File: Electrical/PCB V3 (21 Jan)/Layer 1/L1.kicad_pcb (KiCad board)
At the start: 2 copper layers, 178 x 170 mm, 197 parts, among them J1 Conn_01x04, U2 CD74HC4067SM, U3 CD74HC4067SM, U5 113991054

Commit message: fixed l1 and l3, awaiting vetting
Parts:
- moved LED20 0.30 mm to (141.7, 149.5)
- moved LED12 0.30 mm to (72.0, 135.7)
- moved LED28 0.30 mm to (155.5, 79.9)
- moved LED4 0.30 mm to (85.9, 66.0)
- moved L10 0.30 mm to (67.7, 117.0)
- moved L18 0.30 mm to (122.9, 153.9)
- moved LED26 0.30 mm to (163.0, 98.0)
- moved L2 0.30 mm to (104.6, 61.7)
- moved LED10 0.30 mm to (64.5, 117.6)
- moved LED2 0.30 mm to (104.0, 58.5)
- moved L26 0.30 mm to (159.9, 98.6)
- moved LED18 0.30 mm to (123.6, 157.0)
- moved L31 0.30 mm to (131.8, 64.4)
- moved L15 0.30 mm to (95.8, 151.2)
- moved L23 0.30 mm to (157.2, 125.8)
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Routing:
- net /L1 RX: track 30.8 -> 43.0 mm
- net +3V3: track 163.9 -> 153.5 mm
- net Net-(L29-Pad2): track 4.43 -> 5.33 mm
- net GND: vias 10 -> 238

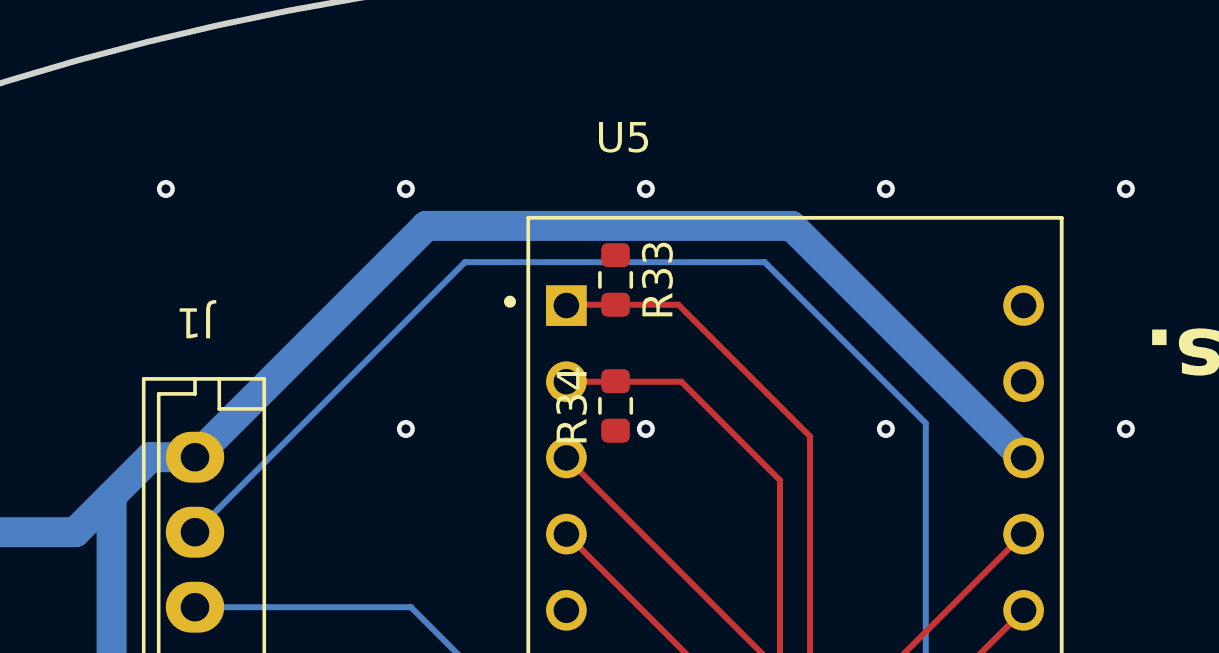
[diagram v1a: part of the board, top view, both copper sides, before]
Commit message: L1 & L3 APPROVED BY HAOYUN
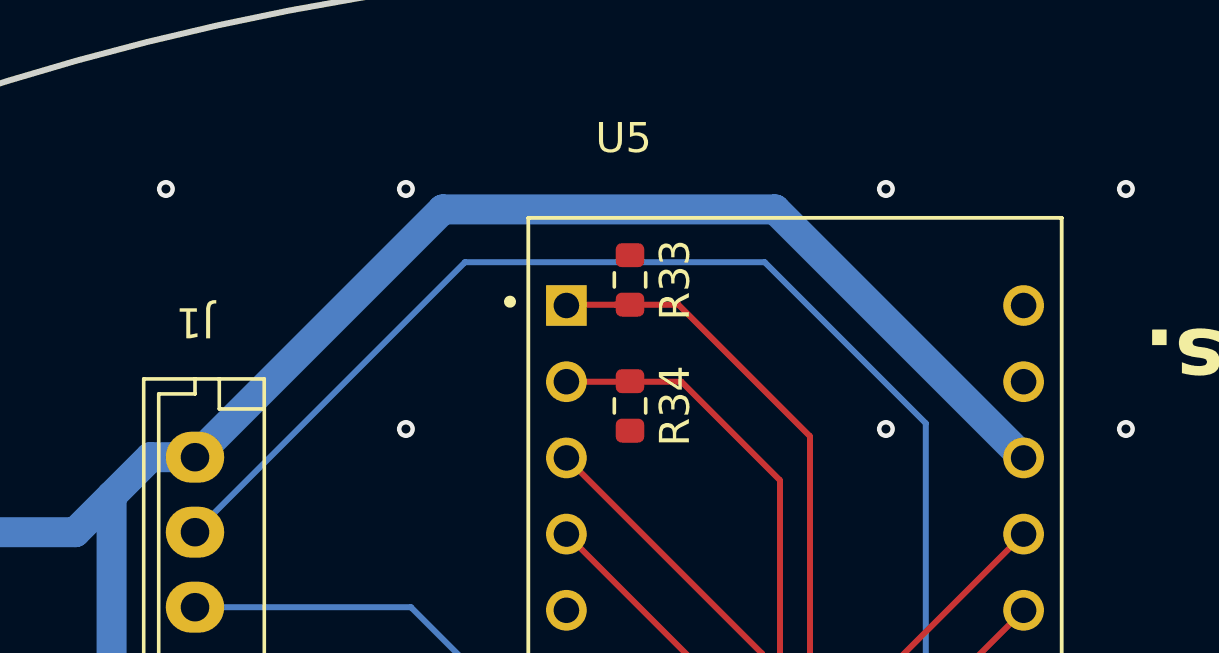
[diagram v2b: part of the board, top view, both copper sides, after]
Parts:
- moved R33 0.48 mm to (108.3, 29.4)
- moved R34 0.48 mm to (108.3, 33.6)
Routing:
- net GND: vias 238 -> 236

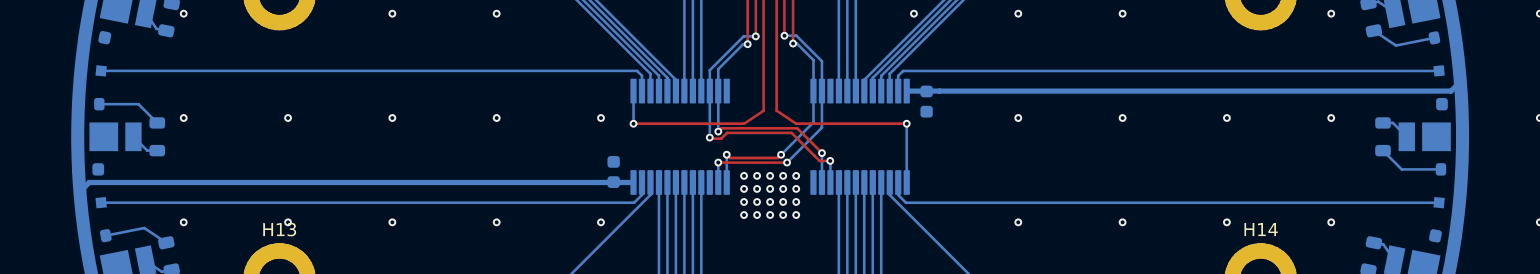
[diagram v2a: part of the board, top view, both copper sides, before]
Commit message: fixed l1 and l3
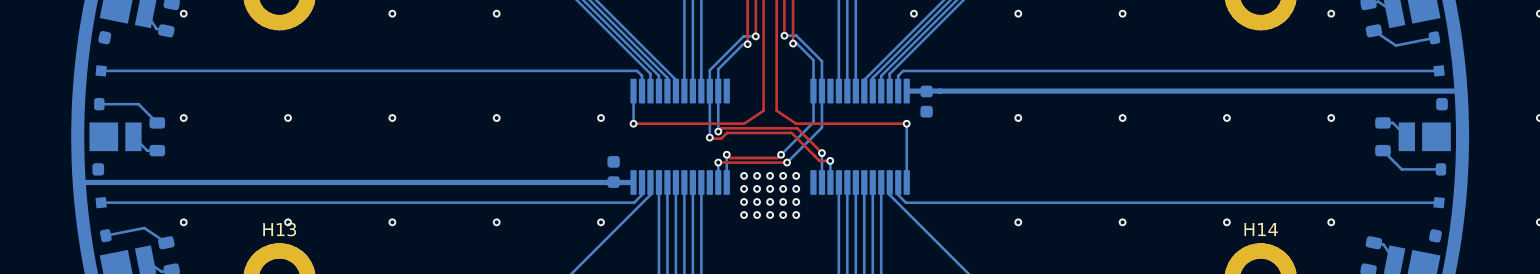
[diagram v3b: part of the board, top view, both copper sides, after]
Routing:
- net +3V3: track 154.0 -> 153.1 mm
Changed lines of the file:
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@@
-	)
-	(segment
-		(start 166.609377 103.65432)
-		(end 165.984377 104.27932)
-		(width 0.4)
-		(layer "B.Cu")
-		(net 2)
 	)
 	(segment
@@
 	)
 	(segment
-		(start 61.554377 111.28932)
+		(start 61.169377 111.28932)
 		(end 103.294374 111.28932)
 		(width 0.4)
@@
 	)
 	(segment
-		(start 60.909377 111.93432)
-		(end 61.554377 111.28932)
-		(width 0.4)
-		(layer "B.Cu")
-		(net 2)
-	)
-	(segment
 		(start 90.989377 59.546741)
 		(end 91.148756 59.70612)
@@
 	)
 	(segment
-		(start 165.984377 104.27932)
+		(start 166.469377 104.27932)
 		(end 126.769377 104.27932)
 		(width 0.4)
@@
 		(layers "F&B.Cu")
 		(hatch edge 0.5)
-		(connect_pads
-			(clearance 0.15)
+		(connect_pads yes
+			(clearance 0.2)
 		)
 		(min_thickness 0.25)
 		(filled_areas_thickness no)
 		(fill yes
-			(thermal_gap 0.5)
+			(thermal_gap 0.2)
 			(thermal_bridge_width 1)
 			(smoothing chamfer)
